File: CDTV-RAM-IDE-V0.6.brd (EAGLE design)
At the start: 80 x 89.2 mm, 56 parts, among them IC2 XC95288XL-TQ144, IC3 74HCT245PW, IC4 74HCT245PW, IC5 74HCT245PW, IC6 AS4C4M16S-6TCN, IC7 LD117AS33TR, IC8 AM29F010J-SOCKET

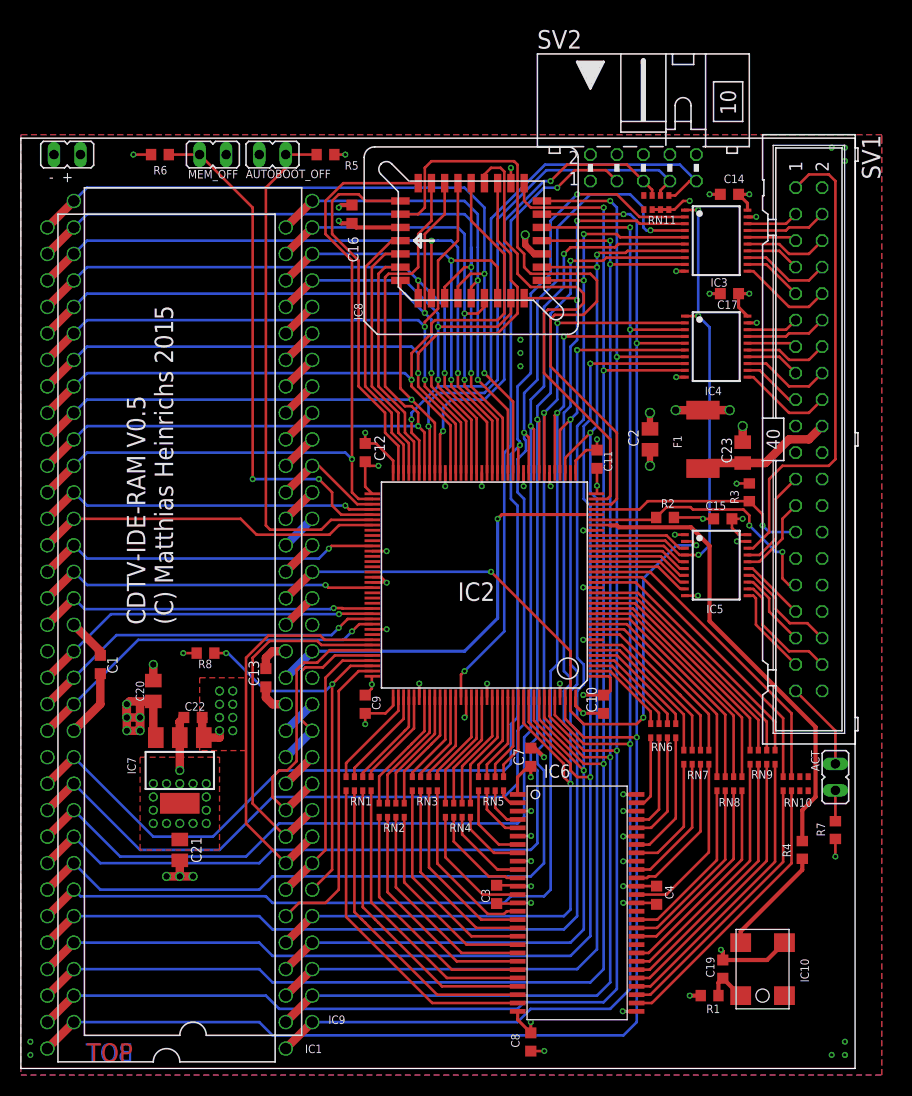
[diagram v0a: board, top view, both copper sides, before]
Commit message: Optimized the PCB and added a Jumper for AT-Bus/Oktapussy
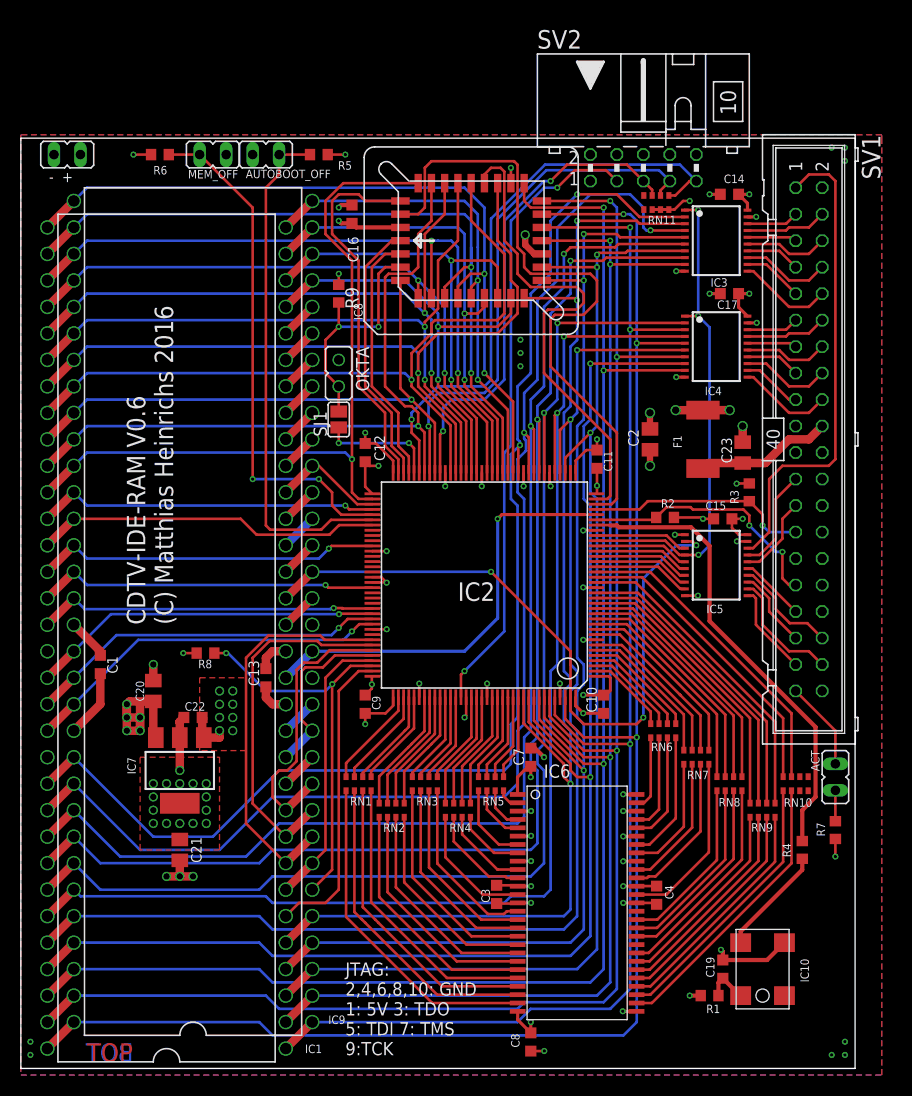
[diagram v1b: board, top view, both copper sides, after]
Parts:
- added OKTA: (no value), jumper:JP1-ROUND
- added R9: 4.7k, rcl:R0603
- added SJ1: (no value), jumper:SJ
- C10, C11, C12, C19, C3, C4, C7, C8, C9: value (none) -> 100n
- F1: value 500mA -> 750mA
- IC10: value (none) -> 50MHz
- R1: value (none) -> FERRITE
- R4: value (none) -> 47
- RN1, RN10, RN2, RN3, RN4, RN5, RN6, RN7, RN8, RN9: value (none) -> 33
- RN11: value (none) -> 4.7k
- moved RN9 5.08 mm to (71.1, 25.4)
- moved R5 0.64 mm to (28.6, 88.3)
- moved AUTOBOOT_OFF 0.63 mm to (23.5, 88.3)
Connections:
- new net N$40: IC2.68, SJ1.1
- net +5V: now also OKTA.1
- net GND: now also R9.1
- net ROM_B0: now also OKTA.2, R9.2, SJ1.2; no longer IC2.68
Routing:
- net N$40: track 0.00 -> 11.3 mm, vias 0 -> 2
- net A_MEM9: track 22.3 -> 27.4 mm
- net A_MEM8: track 23.3 -> 28.3 mm
- net A_MEM7: track 24.2 -> 29.3 mm
- net A_MEM6: track 25.4 -> 30.5 mm
- net N$36: track 27.6 -> 22.5 mm
- net N$35: track 26.4 -> 21.3 mm
- net N$34: track 25.3 -> 20.2 mm
- net N$33: track 24.1 -> 19.1 mm
- net GND: track 93.4 -> 95.1 mm, vias 61 -> 62
- net ROM_B0: track 22.9 -> 22.8 mm, vias 0 -> 2
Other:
- board text added: "CDTV-IDE-RAM V0.6 (C) Matthias Heinrichs 2016"
- board text added: "JTAG: 2,4,6,8,10: GND 1: 5V 3: TDO 5: TDI 7: TMS 9:TCK"
- board text removed: "CDTV-IDE-RAM V0.5 (C) Matthias Heinrichs 2015"
